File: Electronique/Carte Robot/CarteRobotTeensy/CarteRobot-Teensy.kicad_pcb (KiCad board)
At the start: 2 copper layers, 95.5 x 88.5 mm, 31 parts, among them J1 Conn_Bat2, J10 Conn_01x03, J11 Conn_01x05, J12 Conn_01x05, J13 Conn_01x04, J14 Conn_02x04_Counter_Clockwise, J15 Shield-Actionneurs, J19 Conn_IHM, J2 Conn_Bat1, J3 Conn_OnOff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

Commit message: passage Teensy 3.5 + debut lidar
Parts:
- added R4: 390k, Resistor_SMD:R_0805_2012Metric_Pad1.20x1.40mm_HandSolder, F.Cu at (65.0, 120.0)
- added R5: 390k, Resistor_SMD:R_0805_2012Metric_Pad1.20x1.40mm_HandSolder, F.Cu at (67.5, 120.0)
- added R8: 390k, Resistor_SMD:R_0805_2012Metric_Pad1.20x1.40mm_HandSolder, F.Cu at (74.0, 129.0)
- added R9: 390k, Resistor_SMD:R_0805_2012Metric_Pad1.20x1.40mm_HandSolder, F.Cu at (74.0, 126.5)
- J5: value Teensy-3.6 -> Teensy-3.5; footprint Mes_empreintes:Teensy-3.6 -> Mes_empreintes:Teensy-3.5-3.6
- moved J19 39.3 mm to (96.1, 134.0), turned to 180 degrees
- moved J12 19.0 mm to (60.0, 124.6), turned to 90 degrees
- moved J11 14.4 mm to (78.1, 134.0)
- moved J15 3.58 mm to (67.5, 79.5)
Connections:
- J11 pad 3: (no net) -> /CODG_A
- J11 pad 4: (no net) -> /CODG_B
- J15 pad 5: /PWM1 -> +5V
- J15 pad 6: /PWM2 -> /PWM1
- J15 pad 7: /SCL0 -> /PWM2
- J15 pad 8: /SDA0 -> /SCL0
- J5 pad 17: (no net) -> /CODG_A
- J5 pad 18: (no net) -> /CODG_B
- J5 pad 39: (no net) -> /17

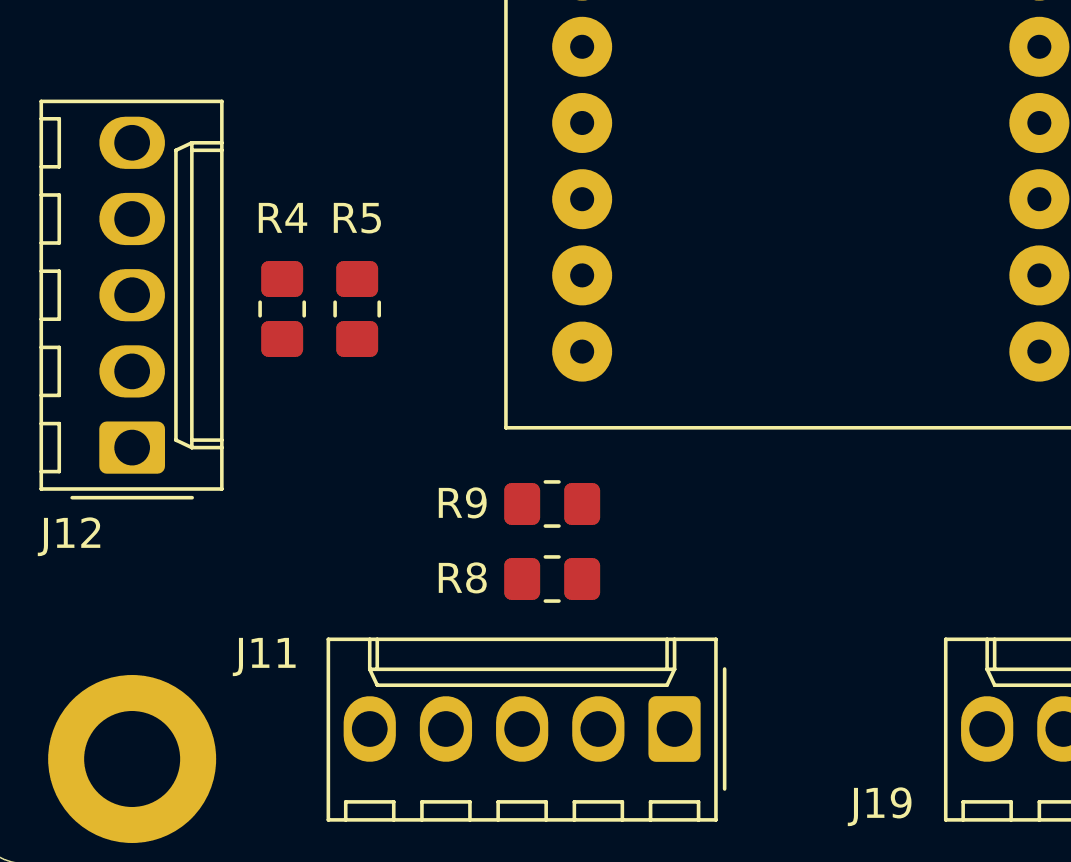
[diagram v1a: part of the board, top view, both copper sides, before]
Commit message: nouvelles pieces lidar
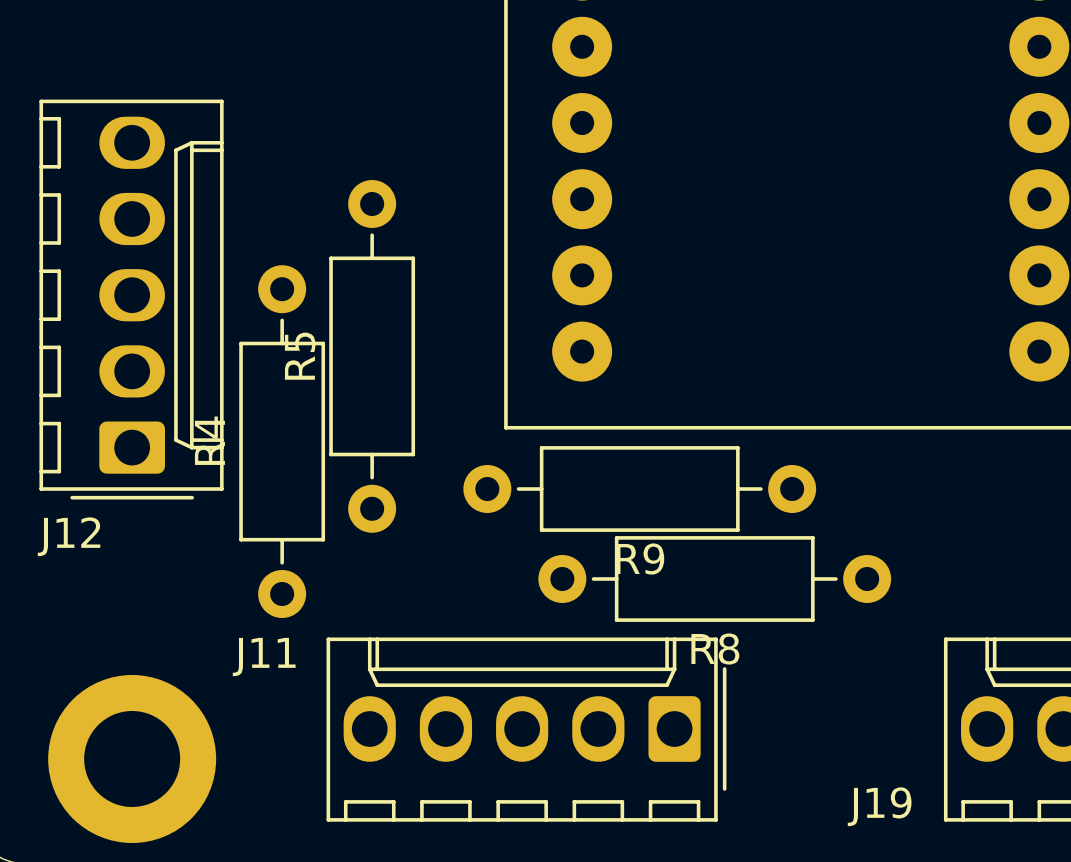
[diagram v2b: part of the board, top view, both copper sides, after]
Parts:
- R4, R5, R8, R9: footprint Resistor_SMD:R_0805_2012Metric_Pad1.20x1.40mm_HandSolder -> Resistor_THT:R_Axial_DIN0207_L6.3mm_D2.5mm_P10.16mm_Horizontal
- moved R8 10.5 mm to (84.5, 129.0)
- moved R4 9.50 mm to (65.0, 129.5)
- moved R9 8.02 mm to (82.0, 126.0)
- moved R5 6.68 mm to (68.0, 126.7)

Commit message: modif elec + meca
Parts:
- added C3: 10u, Capacitor_THT:CP_Radial_D5.0mm_P2.00mm, F.Cu at (63.0, 104.0)
- added J16: Conn_Aru, Connector_Molex:Molex_KK-254_AE-6410-02A_1x02_P2.54mm_Vertical, F.Cu at (137.2, 73.7)
- added J17: Conn_Aru, Connector_Molex:Molex_KK-254_AE-6410-02A_1x02_P2.54mm_Vertical, F.Cu at (137.2, 83.8)
- added J18: Conn_Aru, Connector_Molex:Molex_KK-254_AE-6410-02A_1x02_P2.54mm_Vertical, F.Cu at (146.1, 73.7)
- added J20: Conn_Aru, Connector_Molex:Molex_KK-254_AE-6410-02A_1x02_P2.54mm_Vertical, F.Cu at (146.1, 83.8)
- added J21: Conn_Aru, Connector_Molex:Molex_KK-254_AE-6410-02A_1x02_P2.54mm_Vertical, F.Cu at (102.9, 78.7)
- added R10: 1k, Resistor_THT:R_Axial_DIN0207_L6.3mm_D2.5mm_P10.16mm_Horizontal, F.Cu at (123.0, 75.0)
- added R11: 1k, Resistor_THT:R_Axial_DIN0207_L6.3mm_D2.5mm_P10.16mm_Horizontal, F.Cu at (127.0, 75.0)
- added R12: 4.7k, Resistor_THT:R_Axial_DIN0207_L6.3mm_D2.5mm_P10.16mm_Horizontal, F.Cu at (68.9, 85.9)
- added R13: 4.7k, Resistor_THT:R_Axial_DIN0207_L6.3mm_D2.5mm_P10.16mm_Horizontal, F.Cu at (65.3, 82.8)
- added R6: 1k, Resistor_THT:R_Axial_DIN0207_L6.3mm_D2.5mm_P10.16mm_Horizontal, F.Cu at (115.0, 75.0)
- added R7: 1k, Resistor_THT:R_Axial_DIN0207_L6.3mm_D2.5mm_P10.16mm_Horizontal, F.Cu at (119.0, 75.0)
- C1, C2: footprint Capacitor_THT:CP_Radial_D6.3mm_P2.50mm -> Capacitor_THT:CP_Radial_D5.0mm_P2.50mm
- J15: footprint Mes_empreintes:Adaptateur-Servo-Dynamixel -> Mes_empreintes:Shield-Actionneurs
- J6, J7: footprint Connector_Molex:Molex_KK-254_AE-6410-04A_1x04_P2.54mm_Vertical -> Connector_JST:JST_XH_B4B-XH-A_1x04_P2.50mm_Vertical
- moved J15 9.72 mm to (60.7, 72.6)
- moved C2 2.55 mm to (135.0, 111.0)
- moved C1 0.50 mm to (105.0, 93.0)
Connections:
- J15 pad 1: /Varu -> /SCL2
- J15 pad 10: /17 -> /SCL0
- J15 pad 2: /RX3 -> /SDA2
- J15 pad 3: /TX3 -> /Varu
- J15 pad 5: +5V -> /RX3
- J15 pad 6: /PWM1 -> /TX3
- J15 pad 7: /PWM2 -> +5V
- J15 pad 8: /SCL0 -> /PWM1
- J15 pad 9: /SDA0 -> /PWM2
- J5 pad 20: /CODD_B -> /CE
- J5 pad 21: /CODD_A -> /CODD_B
- J5 pad 22: /CE -> /CODD_A
- J5 pad 35: (no net) -> /MS4
- J5 pad 36: (no net) -> /MS3
- J5 pad 37: (no net) -> /MS2
- J5 pad 38: (no net) -> /MS1
- J5 pad 44: (no net) -> /Tirette
- J5 pad 5: (no net) -> /SCL2
- J5 pad 6: (no net) -> /SDA2

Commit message: routage pcb
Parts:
- added C4: 0,33u, Capacitor_THT:CP_Radial_D5.0mm_P2.00mm, F.Cu at (108.7, 61.5)
- added C5: 0,1u, Capacitor_THT:CP_Radial_D5.0mm_P2.00mm, F.Cu at (101.6, 67.1)
- added D3: LED, LED_THT:LED_D5.0mm_Clear, F.Cu at (61.2, 67.3)
- added J22: Conn_01x03, Connector_PinHeader_2.54mm:PinHeader_1x03_P2.54mm_Vertical, F.Cu at (67.1, 69.6)
- added R14: 500, Resistor_THT:R_Axial_DIN0207_L6.3mm_D2.5mm_P10.16mm_Horizontal, F.Cu at (67.6, 60.7)
- R4, R5, R8, R9: value 390k -> 4.7k
- moved U1 6.47 mm to (113.8, 67.1)
- moved R1 5.08 mm to (120.7, 71.1)
- moved D1 4.77 mm to (126.5, 69.6)
- moved D2 2.71 mm to (127.0, 62.5)
- moved J21 2.54 mm to (102.9, 81.3)
- moved R3 2.43 mm to (100.0, 74.9)
- moved C1 0.98 mm to (104.9, 94.0), turned to 90 degrees
- moved F1 0.60 mm to (112.5, 55.0)
- moved C3 0.51 mm to (63.5, 103.9)
- moved R2 0.48 mm to (96.5, 62.5)
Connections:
- J19 pad 2: /TX4 -> /RX4
- J19 pad 3: /RX4 -> /TX4
- J19 pad 4: /Von -> +5V
- J5 pad 4: (no net) -> /LED
- J5 pad 7: (no net) -> /STRAT
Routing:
- net +5V: track 0.00 -> 201.5 mm
- net +3V3: track 0.00 -> 179.3 mm
- net /Varu: track 0.00 -> 163.0 mm
- net /MS2: track 0.00 -> 62.8 mm
- net /MS4: track 0.00 -> 59.9 mm
- net /MS1: track 0.00 -> 52.3 mm
- net /MS3: track 0.00 -> 50.8 mm
- net /STEP_G: track 0.00 -> 47.1 mm
- net /DIR_G: track 0.00 -> 46.7 mm
- net /EN: track 0.00 -> 44.3 mm
- net Net-(A1-Pad6): track 0.00 -> 43.6 mm
- net /M0: track 0.00 -> 41.8 mm
- net Net-(A1-Pad5): track 0.00 -> 40.3 mm
- net /A1D: track 0.00 -> 36.4 mm
- net /CODG_A: track 0.00 -> 36.0 mm
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- added copper zone on B.Cu, net GND
- added copper zone on F.Cu, net GND

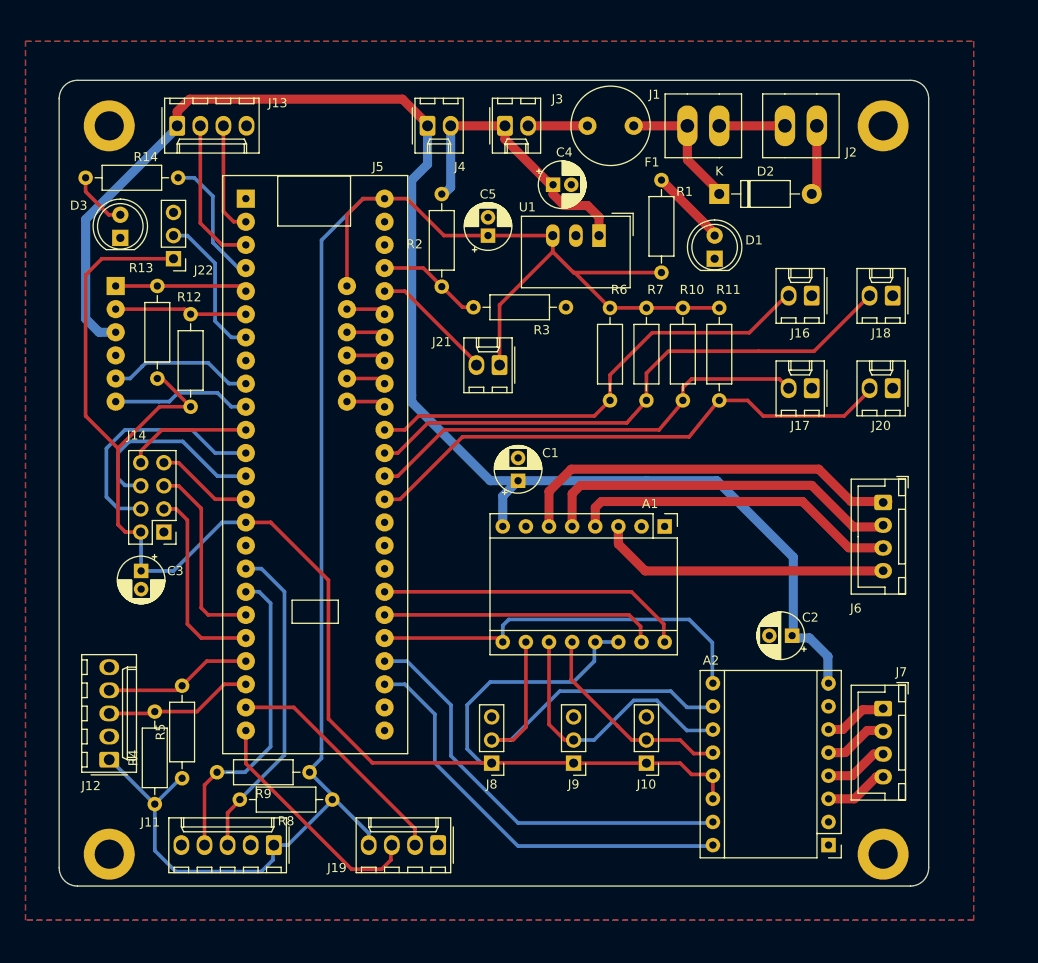
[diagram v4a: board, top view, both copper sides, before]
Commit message: correction carte elec
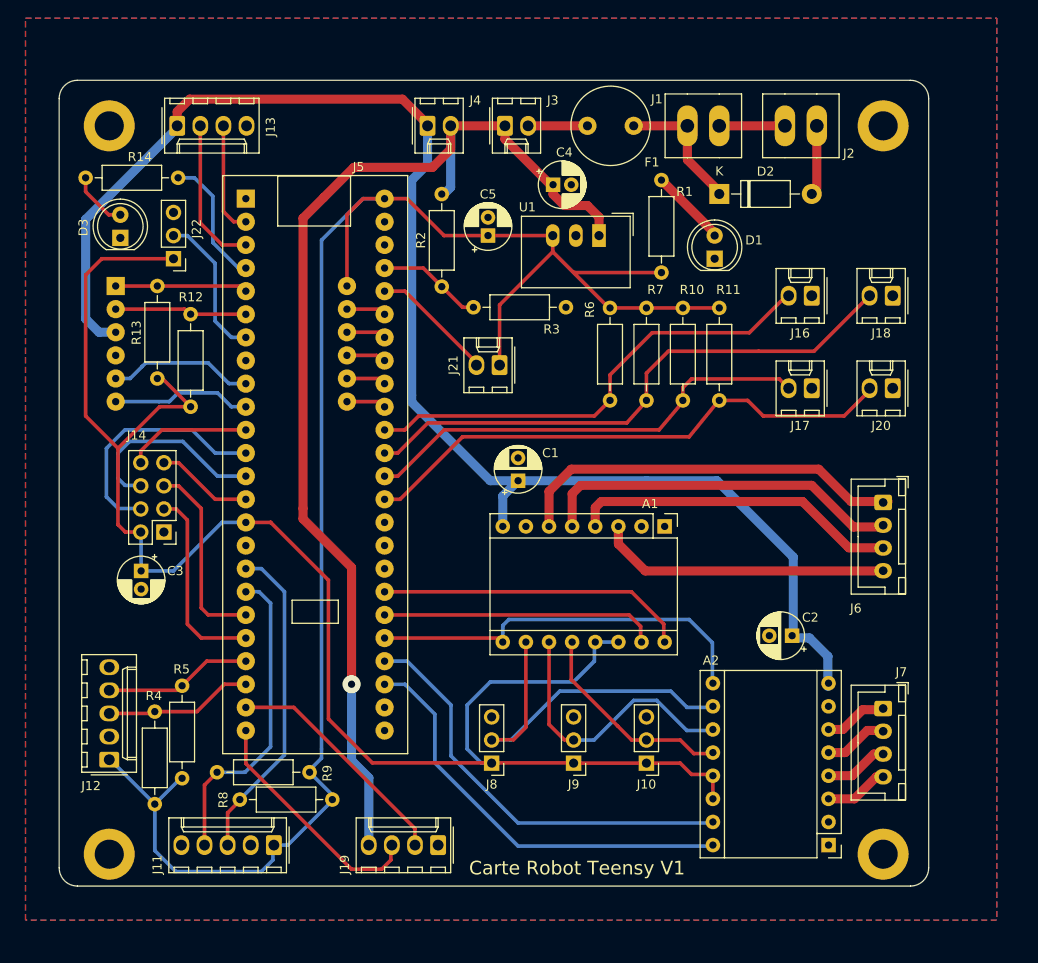
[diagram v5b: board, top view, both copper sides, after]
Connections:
- J19 pad 4: +5V -> /Von
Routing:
- net /Von: track 32.3 -> 126.3 mm, vias 0 -> 1
- net +5V: track 201.5 -> 194.8 mm
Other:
- board text added: "Carte Robot Teensy V1"

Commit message: gerbers
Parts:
- moved J11 1.53 mm to (78.4, 135.5)
- moved J19 1.38 mm to (96.1, 135.4)
- moved R8 1.18 mm to (84.6, 130.2)
- moved R5 0.98 mm to (69.0, 126.5)
- moved R9 0.83 mm to (82.5, 126.6)
- moved R4 0.41 mm to (65.4, 129.5)
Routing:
- net +5V: track 194.8 -> 181.7 mm
- net /CODG_A: track 36.0 -> 37.7 mm
- net /Von: track 126.3 -> 127.8 mm
- net /RX4: track 26.0 -> 27.3 mm
- net /CODD_B: track 16.0 -> 17.1 mm
- net /CODG_B: track 34.7 -> 35.8 mm
- net /TX4: track 26.8 -> 27.7 mm
- net /CODD_A: track 17.1 -> 16.3 mm
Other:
- board size 95.5 x 88.5 mm -> 95.5 x 90 mm

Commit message: info recepteur
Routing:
- removed copper zone on B.Cu, net GND
- removed copper zone on F.Cu, net GND
